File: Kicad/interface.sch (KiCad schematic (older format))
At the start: 16 parts, among them SW1 Push, SW10 Push, SW11 Push, SW12 Push, SW2 Push, SW3 Push, SW4 Push, SW5 Push, SW6 Push, SW7 Push, SW8 Push, SW9 Push, U1 TLC59281DBQ

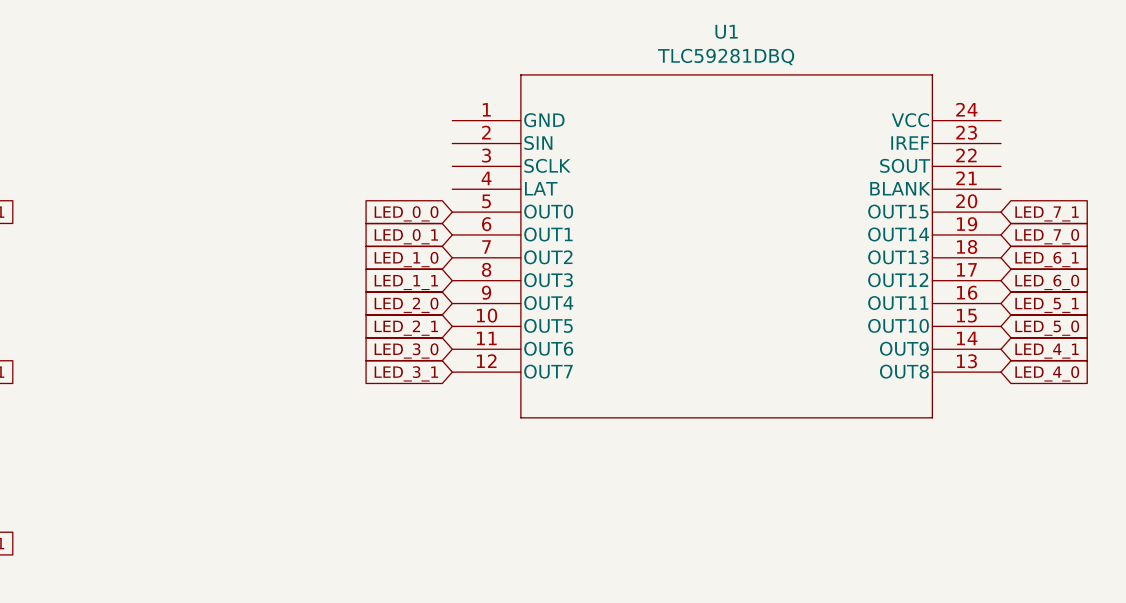
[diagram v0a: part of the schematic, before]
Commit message: added CV output buffers
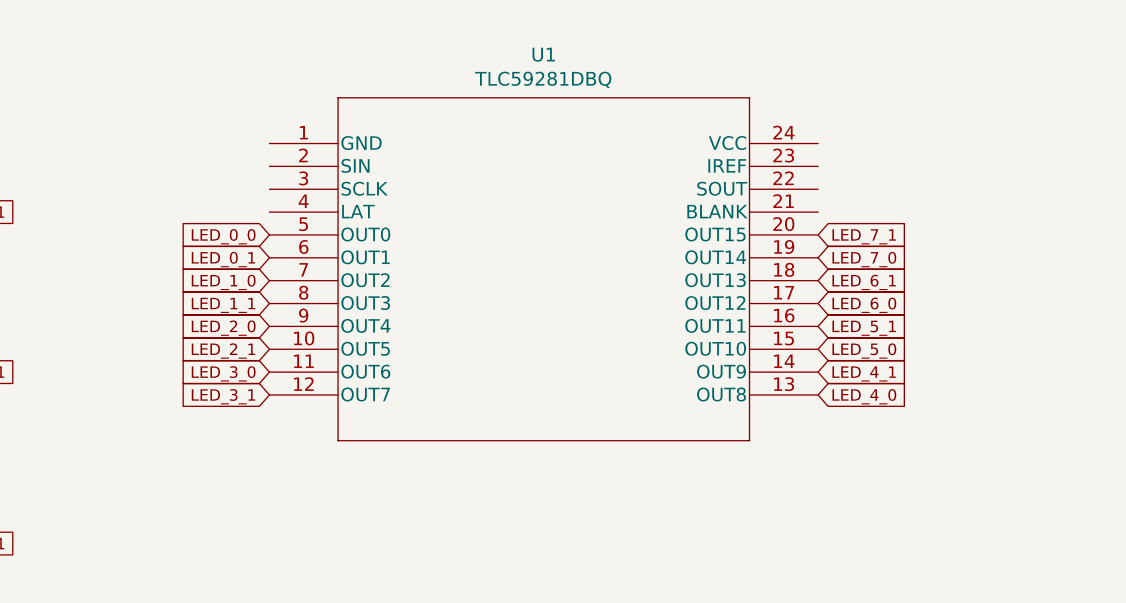
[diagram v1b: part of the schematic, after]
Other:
- moved on the sheet: U1
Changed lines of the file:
@@
 L eurorack_custom:ul_TLC59281DBQ_TLC59281DBQ U?
 U 1 1 5FCB018C
-P 4150 1150
+P 3350 1250
 AR Path="/5FB96D72/5FCB018C" Ref="U?"  Part="1"
 AR Path="/5FC5188F/5FCB018C" Ref="U1"  Part="1"
-F 0 "U1" H 5350 1537 60  0000 C CNN
-F 1 "TLC59281DBQ" H 5350 1431 60  0000 C CNN
-F 2 "Package_DFN_QFN:VQFN-24-1EP_4x4mm_P0.5mm_EP2.45x2.45mm" H 5350 1390 60  0001 C CNN
-F 3 "" H 4150 1150 60  0000 C CNN
-	1    4150 1150
+F 0 "U1" H 4550 1637 60  0000 C CNN
+F 1 "TLC59281DBQ" H 4550 1531 60  0000 C CNN
+F 2 "Package_DFN_QFN:VQFN-24-1EP_4x4mm_P0.5mm_EP2.45x2.45mm" H 4550 1490 60  0001 C CNN
+F 3 "" H 3350 1250 60  0000 C CNN
+	1    3350 1250
 	1    0    0    -1
 $EndComp
@@
 	1    0    0    -1
 $EndComp
-Text GLabel 4150 1550 0    50   Input ~ 0
+Text GLabel 3350 1650 0    50   Input ~ 0
 LED_0_0
-Text GLabel 4150 1650 0    50   Input ~ 0
+Text GLabel 3350 1750 0    50   Input ~ 0
 LED_0_1
-Text GLabel 4150 1750 0    50   Input ~ 0
+Text GLabel 3350 1850 0    50   Input ~ 0
 LED_1_0
-Text GLabel 4150 1850 0    50   Input ~ 0
+Text GLabel 3350 1950 0    50   Input ~ 0
 LED_1_1
-Text GLabel 4150 1950 0    50   Input ~ 0
+Text GLabel 3350 2050 0    50   Input ~ 0
 LED_2_0
-Text GLabel 4150 2050 0    50   Input ~ 0
+Text GLabel 3350 2150 0    50   Input ~ 0
 LED_2_1
-Text GLabel 4150 2150 0    50   Input ~ 0
+Text GLabel 3350 2250 0    50   Input ~ 0
 LED_3_0
-Text GLabel 4150 2250 0    50   Input ~ 0
+Text GLabel 3350 2350 0    50   Input ~ 0
 LED_3_1
-Text GLabel 6550 1550 2    50   Input ~ 0
+Text GLabel 5750 1650 2    50   Input ~ 0
 LED_7_1
-Text GLabel 6550 1650 2    50   Input ~ 0
+Text GLabel 5750 1750 2    50   Input ~ 0
 LED_7_0
-Text GLabel 6550 1750 2    50   Input ~ 0
+Text GLabel 5750 1850 2    50   Input ~ 0
 LED_6_1
-Text GLabel 6550 1850 2    50   Input ~ 0
+Text GLabel 5750 1950 2    50   Input ~ 0
 LED_6_0
-Text GLabel 6550 1950 2    50   Input ~ 0
+Text GLabel 5750 2050 2    50   Input ~ 0
 LED_5_1
-Text GLabel 6550 2050 2    50   Input ~ 0
+Text GLabel 5750 2150 2    50   Input ~ 0
 LED_5_0
-Text GLabel 6550 2150 2    50   Input ~ 0
+Text GLabel 5750 2250 2    50   Input ~ 0
 LED_4_1
-Text GLabel 6550 2250 2    50   Input ~ 0
+Text GLabel 5750 2350 2    50   Input ~ 0
 LED_4_0
 Text GLabel 1550 1550 0    50   Input ~ 0
@@
 U 1 1 5FC83868
 P 4300 4100
+AR Path="/5FC83868" Ref="SW?"  Part="1"
+AR Path="/5FC5188F/5FC83868" Ref="SW?"  Part="1"
 F 0 "SW?" H 4300 4467 50  0000 C CNN
 F 1 "Rotary_Encoder_Switch" H 4300 4376 50  0000 C CNN
@@
 U 1 1 5FC8386E
 P 3350 4100
+AR Path="/5FC8386E" Ref="SW?"  Part="1"
+AR Path="/5FC5188F/5FC8386E" Ref="SW?"  Part="1"
 F 0 "SW?" H 3350 4467 50  0000 C CNN
 F 1 "Rotary_Encoder_Switch" H 3350 4376 50  0000 C CNN
@@
 U 1 1 5FC83874
 P 3350 4800
+AR Path="/5FC83874" Ref="SW?"  Part="1"
+AR Path="/5FC5188F/5FC83874" Ref="SW?"  Part="1"
 F 0 "SW?" H 3350 5167 50  0000 C CNN
 F 1 "Rotary_Encoder_Switch" H 3350 5076 50  0000 C CNN

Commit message: making progress on interface
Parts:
- removed SW? (x2): Rotary_Encoder_Switch, Rotary_Encoder:RotaryEncoder_Alps_EC12E-Switch_Vertical_H20mm, symbol Device:Rotary_Encoder_Switch
- added J? (x2): SN74HC165, symbol eurocad:SN74HC165
- added R? (x12): R_Small, symbol Device:R_Small
- added R? (x3): 10k, symbol Device:R_Small
- added SW13, SW14: Rotary_Encoder_Switch, Rotary_Encoder:RotaryEncoder_Alps_EC12E-Switch_Vertical_H20mm, symbol Device:Rotary_Encoder_Switch
- gave numbers to parts that had none: 1
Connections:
- net +5V: now reaches SW15.S1
- net +5V: now also SW1.1, SW1.6, SW10.1, SW10.6, SW11.1, SW11.6, SW12.1, SW12.6, SW2.1, SW2.6, SW3.1, SW3.6, SW4.1, SW4.6, SW5.1, SW5.6, SW6.1, SW6.6, SW7.1, SW7.6, SW8.1, SW8.6, SW9.1, SW9.6, U1.24 (VCC), J?.16 (VCC), J?.16 (VCC), SW13.S1, SW14.S1
- net SW15: now reaches SW15.S2
- net SW15: now also J?.5 (G), R?.1
- net SW5: now reaches SW5.4
- net SW5: now also J?.3 (E), R?.1
- net SW6: now reaches SW6.4
- net SW6: now also J?.4 (F), R?.1
- net SW3: now reaches SW3.4
- net SW3: now also J?.13 (C), R?.1
- net SW4: now reaches SW4.4
- net SW4: now also J?.14 (D), R?.1
- net LED_11_0: now reaches SW11.2
- net SW11: now reaches SW11.4
- net SW11: now also J?.13 (C), R?.1
- net LED_11_1: now reaches SW11.5
- net LED_12_0: now reaches SW12.2
- net SW12: now reaches SW12.4
- net SW12: now also J?.14 (D), R?.1
- net LED_12_1: now reaches SW12.5
- net GND: now reaches U1.1 (GND)
- net GND: now also J?.8 (GND), J?.8 (GND), R?.2, R?.2, R?.2, R?.2, R?.2, R?.2, R?.2, R?.2, R?.2, R?.2, R?.2, R?.2, R?.2, R?.2, R?.2
- net LED_10_0: now reaches SW10.2
- net SW10: now reaches SW10.4
- net SW10: now also J?.12 (B), R?.1
- net LED_10_1: now reaches SW10.5
- net SW2: now reaches SW2.4
- net SW2: now also J?.12 (B), R?.1
- net LED_9_0: now reaches SW9.2
- net SW9: now reaches SW9.4
- net SW9: now also J?.11 (A), R?.1
- net LED_9_1: now reaches SW9.5
- net SW8: now reaches SW8.4
- net SW8: now also J?.6 (H), R?.1
- net SW7: now reaches SW7.4
- net SW7: now also J?.5 (G), R?.1
- net SW1: now reaches SW1.4
- net SW1: now also J?.11 (A), R?.1
- new net: J?.10 (SER), J?.9 (QH)
- new net SHIFT_REG_CLK: J?.2 (CLK), J?.2 (CLK)
- new net SHIFT_REG_IN: J?.10 (SER)
- new net SW13: J?.3 (E), R?.1, SW13.S2
- new net SW14: J?.4 (F), R?.1, SW14.S2
- no-connect marks 0 -> 3
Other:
- moved on the sheet: SW10, SW11, SW12, SW15, SW9, U1

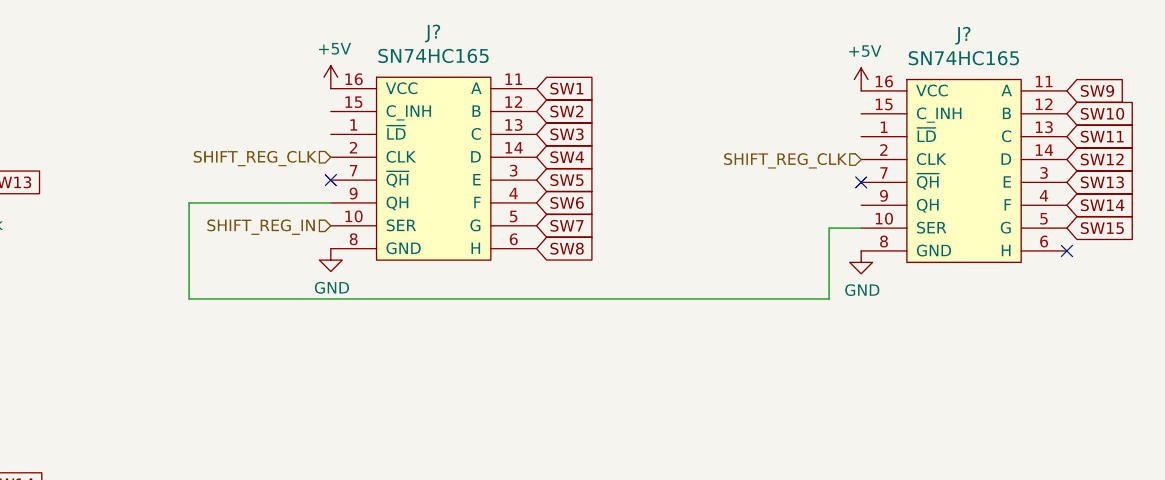
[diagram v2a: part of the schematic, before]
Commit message: connected shift registers for switches
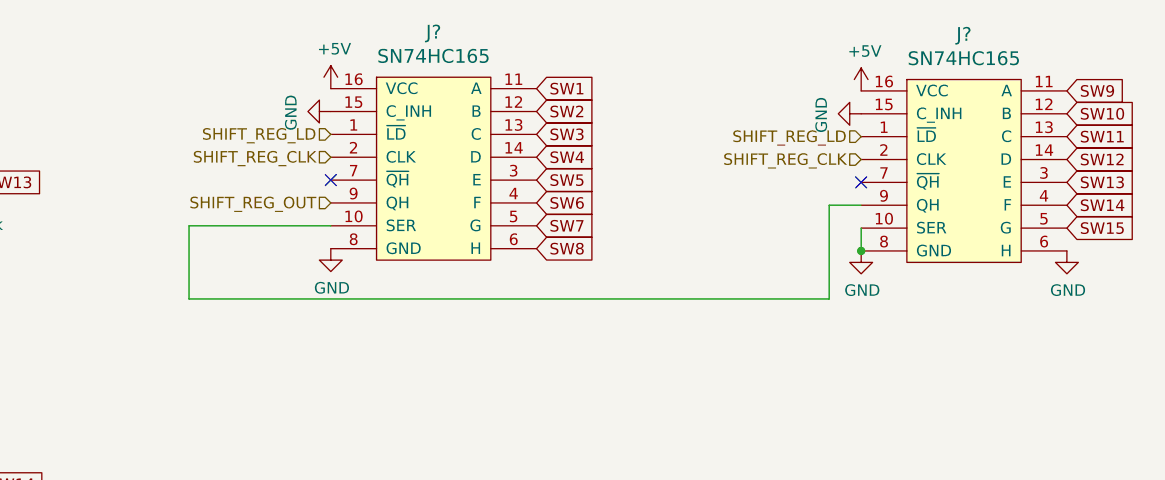
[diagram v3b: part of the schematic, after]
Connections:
- net SHIFT_REG_IN is gone; now on an unnamed net: J?.10 (SER)
- net GND: now also J?.10 (SER), J?.15 (C_INH), J?.15 (C_INH), J?.6 (H)
- net SHIFT_REG_LD: now reaches J?.1 (~LD)
- net SHIFT_REG_LD: now also J?.1 (~LD)
- net SHIFT_REG_OUT: now reaches J?.9 (QH)
- net SHIFT_REG_OUT: no longer J?.10 (SER)
- no-connect marks 3 -> 2
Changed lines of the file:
@@
 Text GLabel 9130 1920 2    50   Input ~ 0
 SW15
-NoConn ~ 9130 2020
 $Comp
 L power:+5V #PWR?
@@
 Connection ~ 4720 6240
 Wire Wire Line
-	5910 1810 5290 1810
-Wire Wire Line
-	5290 1810 5290 2230
-Wire Wire Line
 	5290 2230 8090 2230
-Wire Wire Line
-	8090 2230 8090 1920
-Wire Wire Line
-	8090 1920 8230 1920
-Text HLabel 5910 1910 0    50   Input ~ 0
-SHIFT_REG_IN
+Text HLabel 5910 1810 0    50   Input ~ 0
+SHIFT_REG_OUT
 NoConn ~ 8230 1720
 NoConn ~ 5910 1710
@@
 	0    1    1    0
 $EndComp
+$Comp
+L power:GND #PWR?
+U 1 1 5FC8F2A6
+P 5910 1410
+F 0 "#PWR?" H 5910 1160 50  0001 C CNN
+F 1 "GND" H 5915 1237 50  0000 C CNN
+F 2 "" H 5910 1410 50  0001 C CNN
+F 3 "" H 5910 1410 50  0001 C CNN
+	1    5910 1410
+	0    1    1    0
+$EndComp
+$Comp
+L power:GND #PWR?
+U 1 1 5FC8F7EA
+P 8230 1420
+F 0 "#PWR?" H 8230 1170 50  0001 C CNN
+F 1 "GND" H 8235 1247 50  0000 C CNN
+F 2 "" H 8230 1420 50  0001 C CNN
+F 3 "" H 8230 1420 50  0001 C CNN
+	1    8230 1420
+	0    1    1    0
+$EndComp
+Wire Wire Line
+	5290 2230 5290 1910
+Wire Wire Line
+	5290 1910 5910 1910
+Wire Wire Line
+	8090 1820 8230 1820
+Wire Wire Line
+	8090 1820 8090 2230
+Wire Wire Line
+	8230 1920 8230 2020
+Connection ~ 8230 2020
+Text HLabel 5910 1510 0    50   Input ~ 0
+SHIFT_REG_LD
+Text HLabel 8230 1520 0    50   Input ~ 0
+SHIFT_REG_LD
+$Comp
+L power:GND #PWR?
+U 1 1 5FCB16CE
+P 9130 2020
+F 0 "#PWR?" H 9130 1770 50  0001 C CNN
+F 1 "GND" H 9135 1847 50  0000 C CNN
+F 2 "" H 9130 2020 50  0001 C CNN
+F 3 "" H 9130 2020 50  0001 C CNN
+	1    9130 2020
+	1    0    0    -1
+$EndComp
 $EndSCHEMATC
